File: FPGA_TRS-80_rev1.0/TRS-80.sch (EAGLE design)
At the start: 165 parts, among them IC2 CP2102, U1 EP4CE6E22C8N, X1 PN61729-S

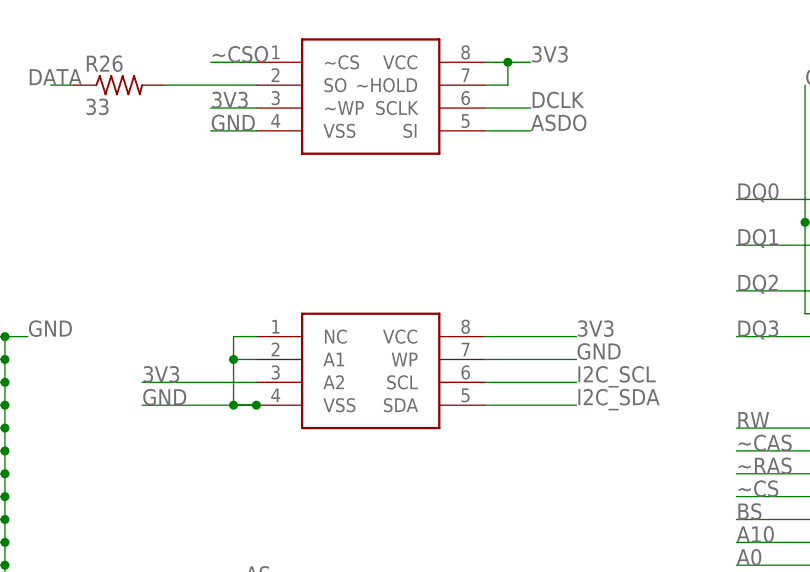
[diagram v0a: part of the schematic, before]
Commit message: fixed HDMI signal names in V2.0, fixed missing I2C resistors in V1.0
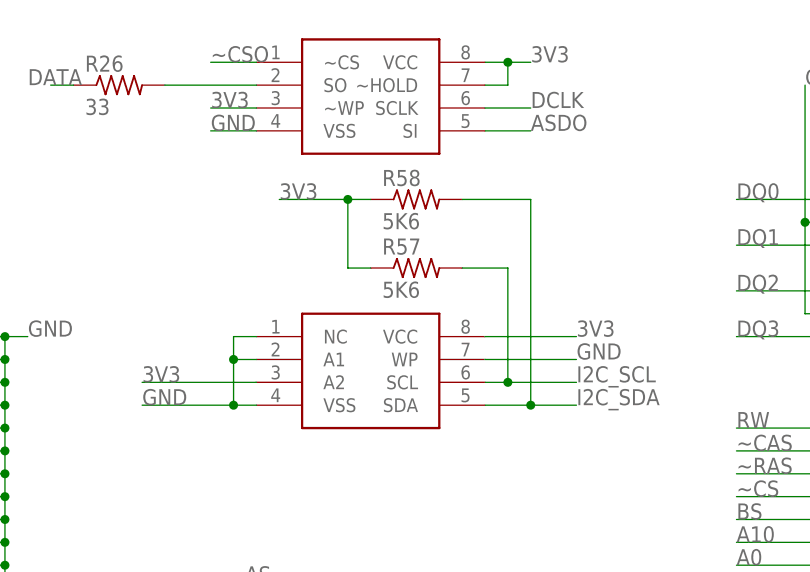
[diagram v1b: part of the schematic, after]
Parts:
- added R57, R58: 5K6, rcl:R-US_R0805
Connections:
- net 3V3: now also R57.1, R58.1
- net I2C_SCL: now also R57.2
- net I2C_SDA: now also R58.2
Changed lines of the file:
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@@
 <part name="R56" library="rcl" deviceset="R-US_" device="R0805" value="2k2"/>
 <part name="POWER" library="Signetics" deviceset="LED_0805" device=""/>
+<part name="R57" library="rcl" deviceset="R-US_" device="R0805" value="5K6"/>
+<part name="R58" library="rcl" deviceset="R-US_" device="R0805" value="5K6"/>
 </parts>
 <sheets>
@@
 <instance part="R56" gate="G$1" x="292.1" y="312.42"/>
 <instance part="POWER" gate="G$1" x="304.8" y="312.42" rot="R90"/>
+<instance part="R57" gate="G$1" x="213.36" y="58.42"/>
+<instance part="R58" gate="G$1" x="213.36" y="66.04"/>
 </instances>
 <busses>
@@
 <junction x="231.14" y="307.34"/>
 </segment>
+<segment>
+<pinref part="R58" gate="G$1" pin="1"/>
+<wire x1="208.28" y1="66.04" x2="205.74" y2="66.04" width="0.1524" layer="91"/>
+<pinref part="R57" gate="G$1" pin="1"/>
+<wire x1="205.74" y1="66.04" x2="198.12" y2="66.04" width="0.1524" layer="91"/>
+<wire x1="208.28" y1="58.42" x2="205.74" y2="58.42" width="0.1524" layer="91"/>
+<wire x1="205.74" y1="58.42" x2="205.74" y2="66.04" width="0.1524" layer="91"/>
+<junction x="205.74" y="66.04"/>
+<label x="198.12" y="66.04" size="1.778" layer="95"/>
+</segment>
 </net>
 <net name="2V5" class="0">
@@
 <segment>
 <pinref part="U$17" gate="G$1" pin="SCL"/>
-<wire x1="220.98" y1="45.72" x2="231.14" y2="45.72" width="0.1524" layer="91"/>
+<wire x1="220.98" y1="45.72" x2="223.52" y2="45.72" width="0.1524" layer="91"/>
 <label x="231.14" y="45.72" size="1.778" layer="95"/>
+<pinref part="R57" gate="G$1" pin="2"/>
+<wire x1="223.52" y1="45.72" x2="231.14" y2="45.72" width="0.1524" layer="91"/>
+<wire x1="218.44" y1="58.42" x2="223.52" y2="58.42" width="0.1524" layer="91"/>
+<wire x1="223.52" y1="58.42" x2="223.52" y2="45.72" width="0.1524" layer="91"/>
+<junction x="223.52" y="45.72"/>
 </segment>
 <segment>
@@
 <segment>
 <pinref part="U$17" gate="G$1" pin="SDA"/>
-<wire x1="220.98" y1="43.18" x2="231.14" y2="43.18" width="0.1524" layer="91"/>
+<wire x1="220.98" y1="43.18" x2="226.06" y2="43.18" width="0.1524" layer="91"/>
 <label x="231.14" y="43.18" size="1.778" layer="95"/>
+<pinref part="R58" gate="G$1" pin="2"/>
+<wire x1="226.06" y1="43.18" x2="231.14" y2="43.18" width="0.1524" layer="91"/>
+<wire x1="218.44" y1="66.04" x2="226.06" y2="66.04" width="0.1524" layer="91"/>
+<wire x1="226.06" y1="66.04" x2="226.06" y2="43.18" width="0.1524" layer="91"/>
+<junction x="226.06" y="43.18"/>
 </segment>
 <segment>
@@
 <pinref part="U$17" gate="G$1" pin="VSS"/>
 <wire x1="193.04" y1="48.26" x2="193.04" y2="43.18" width="0.1524" layer="91"/>
-<wire x1="193.04" y1="43.18" x2="195.58" y2="43.18" width="0.1524" layer="91"/>
 <wire x1="195.58" y1="43.18" x2="193.04" y2="43.18" width="0.1524" layer="91"/>
 <pinref part="U$17" gate="G$1" pin="A1"/>
@@
 <junction x="193.04" y="48.26"/>
 <junction x="193.04" y="43.18"/>
-<junction x="195.58" y="43.18"/>
-</segment>
-<segment>
+</segment>
+<segment>
